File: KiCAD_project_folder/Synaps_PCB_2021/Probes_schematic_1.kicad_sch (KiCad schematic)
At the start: 28 parts, among them U3 LTC2452ITS8-TRMPBF, U4 LTC2452ITS8-TRMPBF, U5 LTC2452ITS8-TRMPBF, U6 LTC2452ITS8-TRMPBF

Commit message: Added library for one piece
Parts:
- renumbered C35 to C12, C36 to C13, C37 to C14, C38 to C15, C39 to C16, C40 to C17, C41 to C18, C42 to C19, C43 to C20, C44 to C21, C45 to C22, C46 to C23, C47 to C24, C48 to C25, C49 to C26, C50 to C27, C51 to C28, C52 to C29, C53 to C30, C54 to C31, C55 to C32, C56 to C33, C57 to C34, C58 to C35, U4 to U?, U5 to U?, U6 to U?, U3 to U?

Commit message: Added LTC2452 librairy
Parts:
- removed U? (x4): LTC2452ITS8-TRMPBF, TSOT-23_TS8_LIT, symbol 2021-11-05_00-54-21:LTC2452ITS8-TRMPBF
- added U3, U4, U5, U6: LTC2452ITS8-TRMPBF, TSOT-23_TS8_LIT, symbol LTC2452:LTC2452ITS8-TRMPBF
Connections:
- net +3V3: now also U3.3 (REF), U3.4 (VCC), U4.3 (REF), U4.4 (VCC), U5.3 (REF), U5.4 (VCC), U6.3 (REF), U6.4 (VCC)
- net GNDREF: now also U3.2 (GND), U3.8 (SDO), U4.2 (GND), U4.8 (SDO), U5.2 (GND), U5.8 (SDO), U6.2 (GND), U6.8 (SDO)
- net Probe1_SDO: now also U3.7 (*CS), U4.7 (*CS), U5.7 (*CS), U6.7 (*CS)
- net Probe1_~{CS}: now also U3.6 (IN+), U4.6 (IN+), U5.6 (IN+), U6.6 (IN+)
- net Probe_SCK: now also U3.1 (SCK), U4.1 (SCK), U5.1 (SCK), U6.1 (SCK)
- net sense_+: now also U3.5 (IN-), U4.5 (IN-), U5.5 (IN-), U6.5 (IN-)
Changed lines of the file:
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@@
     (pin "1")
   )
-  (symbol (lib_id "2021-11-05_00-54-21:LTC2452ITS8-TRMPBF") (at 182.88 39.37 0) (unit 1)
-    (in_bom yes) (on_board yes)
-    (property "Reference" "U?" (id 0) (at 210.82 29.5402 0)
+  (symbol (lib_id "LTC2452:LTC2452ITS8-TRMPBF") (at 53.34 162.56 0) (unit 1)
+    (in_bom yes) (on_board yes) (fields_autoplaced)
+    (property "Reference" "U3" (id 0) (at 81.28 153.3324 0)
       (effects (font (size 1.524 1.524)))
     )
-    (property "Value" "LTC2452ITS8-TRMPBF" (id 1) (at 210.82 32.2326 0)
+    (property "Value" "LTC2452ITS8-TRMPBF" (id 1) (at 81.28 156.3258 0)
+      (effects (font (size 1.524 1.524)))
+    )
+    (property "Footprint" "TSOT-23_TS8_LIT" (id 2) (at 81.28 156.464 0)
+      (effects (font (size 1.524 1.524)) hide)
+    )
+    (property "Datasheet" "" (id 3) (at 53.34 162.56 0)
+      (effects (font (size 1.524 1.524)))
+    )
+    (pin "1")
+    (pin "2")
+    (pin "3")
+    (pin "4")
+    (pin "5")
+    (pin "6")
+    (pin "7")
+    (pin "8")
+  )
+  (symbol (lib_id "LTC2452:LTC2452ITS8-TRMPBF") (at 182.88 134.62 0) (unit 1)
+    (in_bom yes) (on_board yes) (fields_autoplaced)
+    (property "Reference" "U6" (id 0) (at 210.82 125.3924 0)
+      (effects (font (size 1.524 1.524)))
+    )
+    (property "Value" "LTC2452ITS8-TRMPBF" (id 1) (at 210.82 128.3858 0)
+      (effects (font (size 1.524 1.524)))
+    )
+    (property "Footprint" "TSOT-23_TS8_LIT" (id 2) (at 210.82 128.524 0)
+      (effects (font (size 1.524 1.524)) hide)
+    )
+    (property "Datasheet" "" (id 3) (at 182.88 134.62 0)
+      (effects (font (size 1.524 1.524)))
+    )
+    (pin "1")
+    (pin "2")
+    (pin "3")
+    (pin "4")
+    (pin "5")
+    (pin "6")
+    (pin "7")
+    (pin "8")
+  )
+  (symbol (lib_id "LTC2452:LTC2452ITS8-TRMPBF") (at 182.88 88.9 0) (unit 1)
+    (in_bom yes) (on_board yes) (fields_autoplaced)
+    (property "Reference" "U5" (id 0) (at 210.82 79.6724 0)
+      (effects (font (size 1.524 1.524)))
+    )
+    (property "Value" "LTC2452ITS8-TRMPBF" (id 1) (at 210.82 82.6658 0)
+      (effects (font (size 1.524 1.524)))
+    )
+    (property "Footprint" "TSOT-23_TS8_LIT" (id 2) (at 210.82 82.804 0)
+      (effects (font (size 1.524 1.524)) hide)
+    )
+    (property "Datasheet" "" (id 3) (at 182.88 88.9 0)
+      (effects (font (size 1.524 1.524)))
+    )
+    (pin "1")
+    (pin "2")
+    (pin "3")
+    (pin "4")
+    (pin "5")
+    (pin "6")
+    (pin "7")
+    (pin "8")
+  )
+  (symbol (lib_id "LTC2452:LTC2452ITS8-TRMPBF") (at 182.88 39.37 0) (unit 1)
+    (in_bom yes) (on_board yes) (fields_autoplaced)
+    (property "Reference" "U4" (id 0) (at 210.82 30.1424 0)
+      (effects (font (size 1.524 1.524)))
+    )
+    (property "Value" "LTC2452ITS8-TRMPBF" (id 1) (at 210.82 33.1358 0)
       (effects (font (size 1.524 1.524)))
     )
@@
       (effects (font (size 1.524 1.524)))
     )
-  )
-  (symbol (lib_id "2021-11-05_00-54-21:LTC2452ITS8-TRMPBF") (at 182.88 88.9 0) (unit 1)
-    (in_bom yes) (on_board yes)
-    (property "Reference" "U?" (id 0) (at 210.82 79.0702 0)
-      (effects (font (size 1.524 1.524)))
-    )
-    (property "Value" "LTC2452ITS8-TRMPBF" (id 1) (at 210.82 81.7626 0)
-      (effects (font (size 1.524 1.524)))
-    )
-    (property "Footprint" "TSOT-23_TS8_LIT" (id 2) (at 210.82 82.804 0)
-      (effects (font (size 1.524 1.524)) hide)
-    )
-    (property "Datasheet" "" (id 3) (at 182.88 88.9 0)
-      (effects (font (size 1.524 1.524)))
-    )
-  )
-  (symbol (lib_id "2021-11-05_00-54-21:LTC2452ITS8-TRMPBF") (at 182.88 134.62 0) (unit 1)
-    (in_bom yes) (on_board yes)
-    (property "Reference" "U?" (id 0) (at 210.82 124.7902 0)
-      (effects (font (size 1.524 1.524)))
-    )
-    (property "Value" "LTC2452ITS8-TRMPBF" (id 1) (at 210.82 127.4826 0)
-      (effects (font (size 1.524 1.524)))
-    )
-    (property "Footprint" "TSOT-23_TS8_LIT" (id 2) (at 210.82 128.524 0)
-      (effects (font (size 1.524 1.524)) hide)
-    )
-    (property "Datasheet" "" (id 3) (at 182.88 134.62 0)
-      (effects (font (size 1.524 1.524)))
-    )
-  )
-  (symbol (lib_id "2021-11-05_00-54-21:LTC2452ITS8-TRMPBF") (at 53.34 162.56 0) (unit 1)
-    (in_bom yes) (on_board yes)
-    (property "Reference" "U?" (id 0) (at 81.28 152.7302 0)
-      (effects (font (size 1.524 1.524)))
-    )
-    (property "Value" "LTC2452ITS8-TRMPBF" (id 1) (at 81.28 155.4226 0)
-      (effects (font (size 1.524 1.524)))
-    )
-    (property "Footprint" "TSOT-23_TS8_LIT" (id 2) (at 81.28 156.464 0)
-      (effects (font (size 1.524 1.524)) hide)
-    )
-    (property "Datasheet" "" (id 3) (at 53.34 162.56 0)
-      (effects (font (size 1.524 1.524)))
-    )
+    (pin "1")
+    (pin "2")
+    (pin "3")
+    (pin "4")
+    (pin "5")
+    (pin "6")
+    (pin "7")
+    (pin "8")
   )
 )

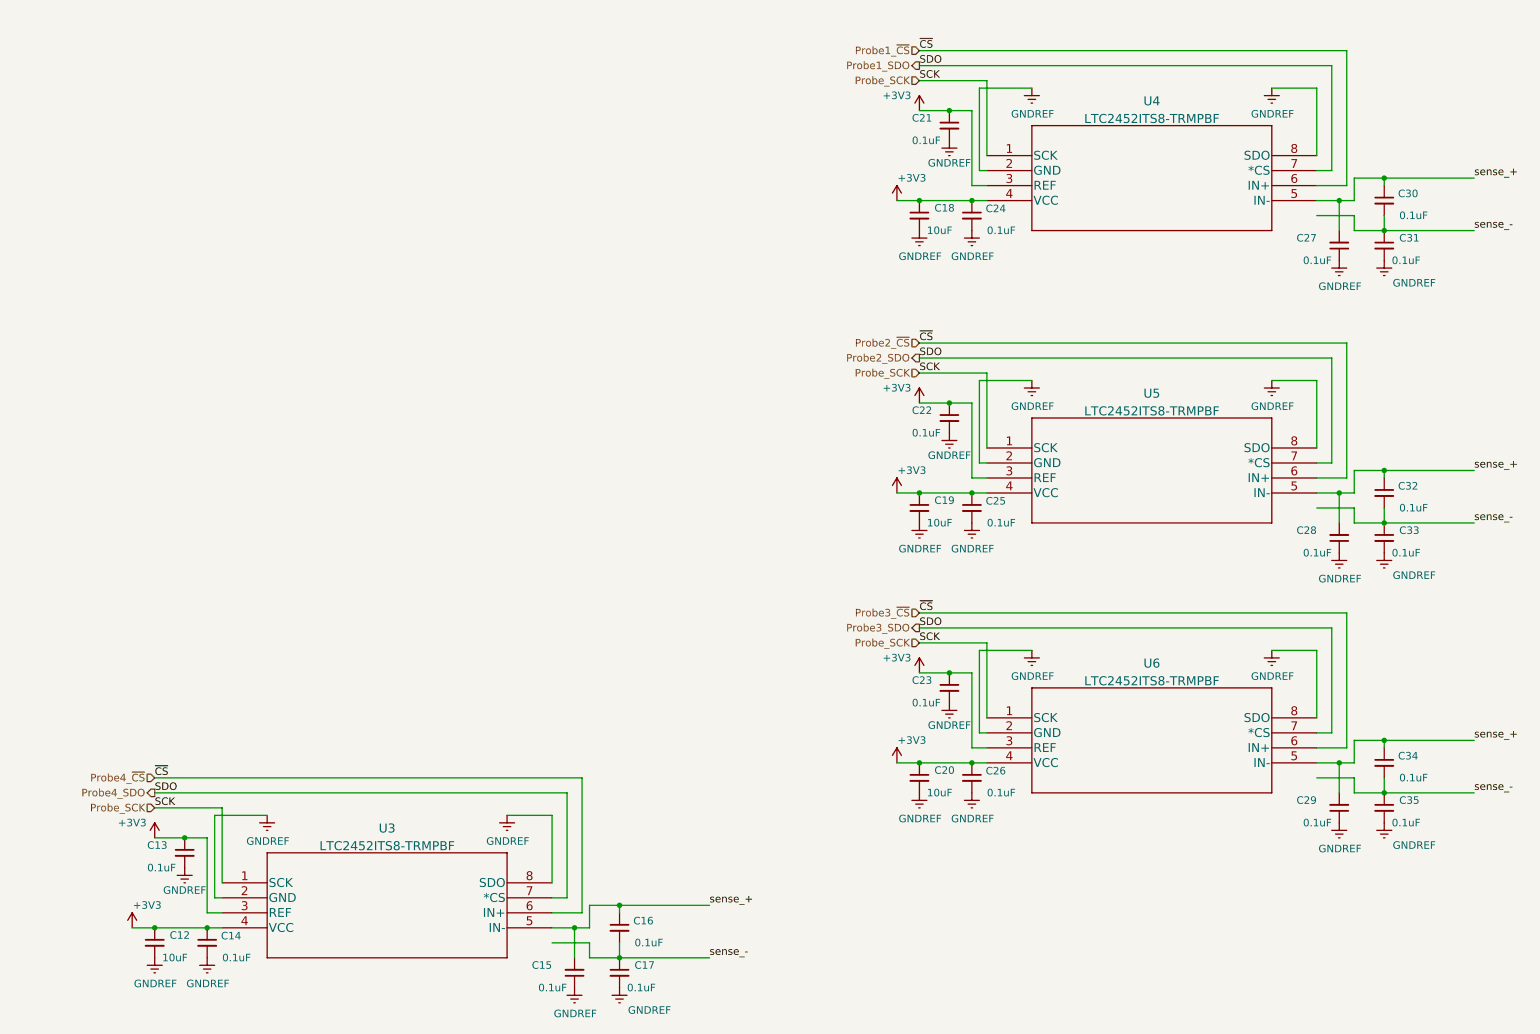
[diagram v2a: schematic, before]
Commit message: Inertia measurement unit schematic
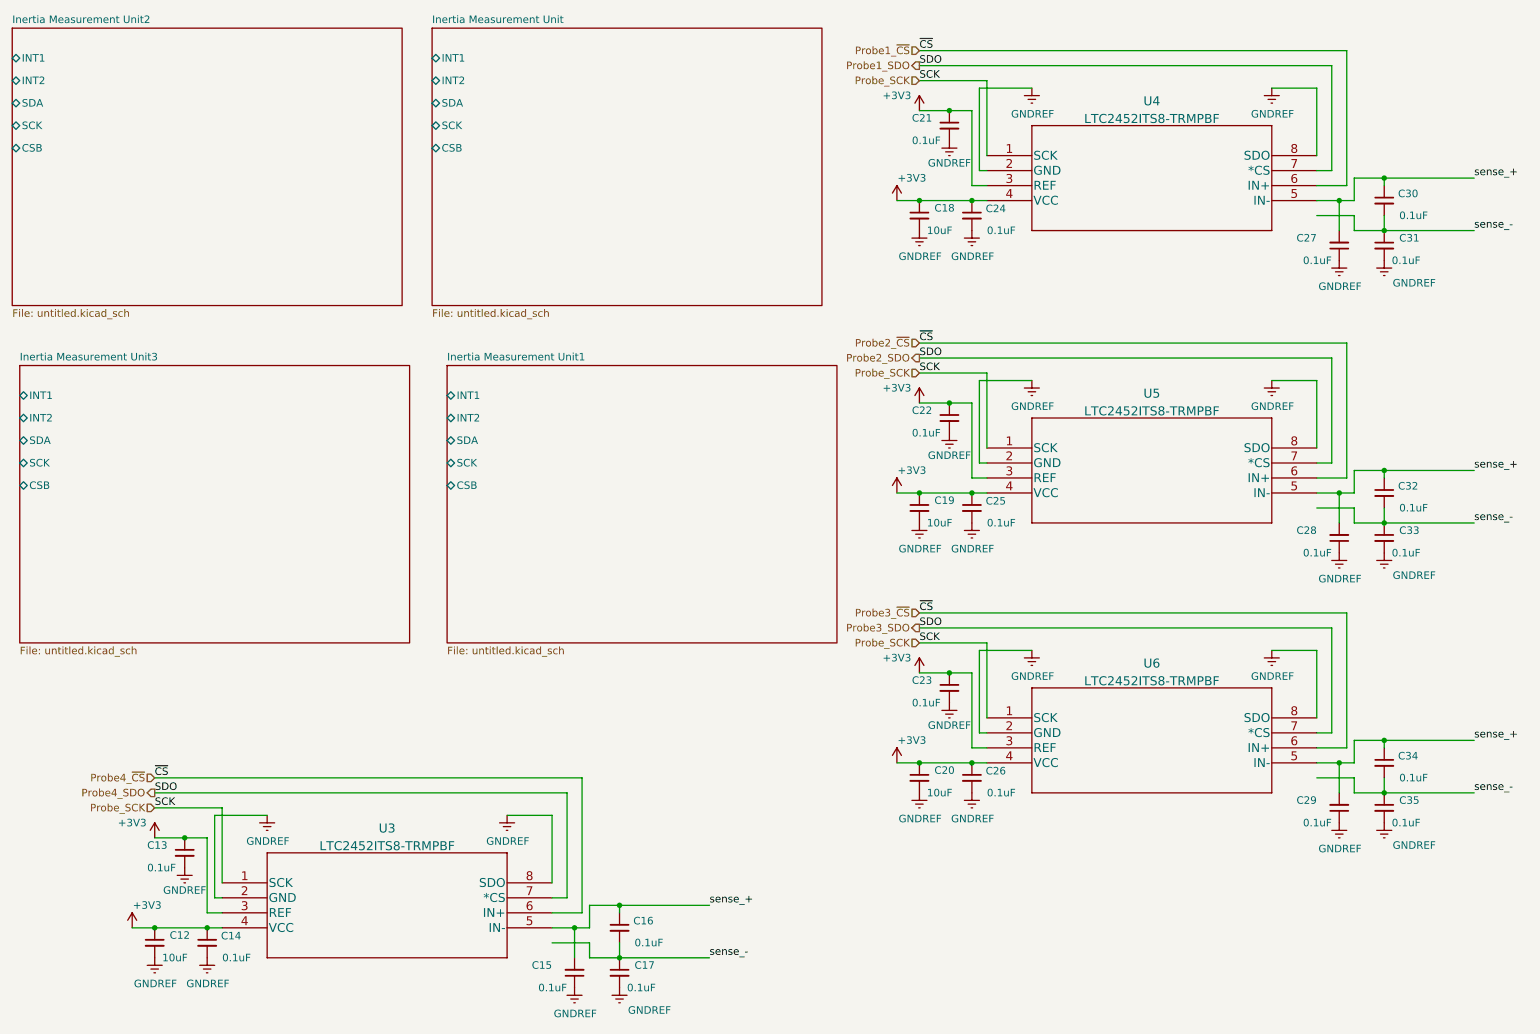
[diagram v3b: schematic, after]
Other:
- added sheet Inertia Measurement Unit (untitled.kicad_sch)
- added sheet Inertia Measurement Unit1 (untitled.kicad_sch)
- added sheet Inertia Measurement Unit2 (untitled.kicad_sch)
- added sheet Inertia Measurement Unit3 (untitled.kicad_sch)
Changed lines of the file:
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@@
     (pin "8")
   )
+  (sheet (at 88.9 17.78) (size 66.04 46.99) (fields_autoplaced)
+    (stroke (width 0.1524) (type solid) (color 0 0 0 0))
+    (fill (color 0 0 0 0.0000))
+    (property "Sheet name" "Inertia Measurement Unit" (id 0) (at 88.9 17.0684 0)
+      (effects (font (size 1.27 1.27)) (justify left bottom))
+    )
+    (property "Sheet file" "untitled.kicad_sch" (id 1) (at 88.9 65.3546 0)
+      (effects (font (size 1.27 1.27)) (justify left top))
+    )
+    (pin "INT1" bidirectional (at 88.9 22.86 180)
+      (effects (font (size 1.27 1.27)) (justify left))
+    )
+    (pin "INT2" bidirectional (at 88.9 26.67 180)
+      (effects (font (size 1.27 1.27)) (justify left))
+    )
+    (pin "SDA" bidirectional (at 88.9 30.48 180)
+      (effects (font (size 1.27 1.27)) (justify left))
+    )
+    (pin "SCK" bidirectional (at 88.9 34.29 180)
+      (effects (font (size 1.27 1.27)) (justify left))
+    )
+    (pin "CSB" bidirectional (at 88.9 38.1 180)
+      (effects (font (size 1.27 1.27)) (justify left))
+    )
+  )
+  (sheet (at 17.78 17.78) (size 66.04 46.99) (fields_autoplaced)
+    (stroke (width 0.1524) (type solid) (color 0 0 0 0))
+    (fill (color 0 0 0 0.0000))
+    (property "Sheet name" "Inertia Measurement Unit2" (id 0) (at 17.78 17.0684 0)
+      (effects (font (size 1.27 1.27)) (justify left bottom))
+    )
+    (property "Sheet file" "untitled.kicad_sch" (id 1) (at 17.78 65.3546 0)
+      (effects (font (size 1.27 1.27)) (justify left top))
+    )
+    (pin "INT1" bidirectional (at 17.78 22.86 180)
+      (effects (font (size 1.27 1.27)) (justify left))
+    )
+    (pin "INT2" bidirectional (at 17.78 26.67 180)
+      (effects (font (size 1.27 1.27)) (justify left))
+    )
+    (pin "SDA" bidirectional (at 17.78 30.48 180)
+      (effects (font (size 1.27 1.27)) (justify left))
+    )
+    (pin "SCK" bidirectional (at 17.78 34.29 180)
+      (effects (font (size 1.27 1.27)) (justify left))
+    )
+    (pin "CSB" bidirectional (at 17.78 38.1 180)
+      (effects (font (size 1.27 1.27)) (justify left))
+    )
+  )
+  (sheet (at 91.44 74.93) (size 66.04 46.99) (fields_autoplaced)
+    (stroke (width 0.1524) (type solid) (color 0 0 0 0))
+    (fill (color 0 0 0 0.0000))
+    (property "Sheet name" "Inertia Measurement Unit1" (id 0) (at 91.44 74.2184 0)
+      (effects (font (size 1.27 1.27)) (justify left bottom))
+    )
+    (property "Sheet file" "untitled.kicad_sch" (id 1) (at 91.44 122.5046 0)
+      (effects (font (size 1.27 1.27)) (justify left top))
+    )
+    (pin "INT1" bidirectional (at 91.44 80.01 180)
+      (effects (font (size 1.27 1.27)) (justify left))
+    )
+    (pin "INT2" bidirectional (at 91.44 83.82 180)
+      (effects (font (size 1.27 1.27)) (justify left))
+    )
+    (pin "SDA" bidirectional (at 91.44 87.63 180)
+      (effects (font (size 1.27 1.27)) (justify left))
+    )
+    (pin "SCK" bidirectional (at 91.44 91.44 180)
+      (effects (font (size 1.27 1.27)) (justify left))
+    )
+    (pin "CSB" bidirectional (at 91.44 95.25 180)
+      (effects (font (size 1.27 1.27)) (justify left))
+    )
+  )
+  (sheet (at 19.05 74.93) (size 66.04 46.99) (fields_autoplaced)
+    (stroke (width 0.1524) (type solid) (color 0 0 0 0))
+    (fill (color 0 0 0 0.0000))
+    (property "Sheet name" "Inertia Measurement Unit3" (id 0) (at 19.05 74.2184 0)
+      (effects (font (size 1.27 1.27)) (justify left bottom))
+    )
+    (property "Sheet file" "untitled.kicad_sch" (id 1) (at 19.05 122.5046 0)
+      (effects (font (size 1.27 1.27)) (justify left top))
+    )
+    (pin "INT1" bidirectional (at 19.05 80.01 180)
+      (effects (font (size 1.27 1.27)) (justify left))
+    )
+    (pin "INT2" bidirectional (at 19.05 83.82 180)
+      (effects (font (size 1.27 1.27)) (justify left))
+    )
+    (pin "SDA" bidirectional (at 19.05 87.63 180)
+      (effects (font (size 1.27 1.27)) (justify left))
+    )
+    (pin "SCK" bidirectional (at 19.05 91.44 180)
+      (effects (font (size 1.27 1.27)) (justify left))
+    )
+    (pin "CSB" bidirectional (at 19.05 95.25 180)
+      (effects (font (size 1.27 1.27)) (justify left))
+    )
+  )
 )

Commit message: Added basic PCB guidelines
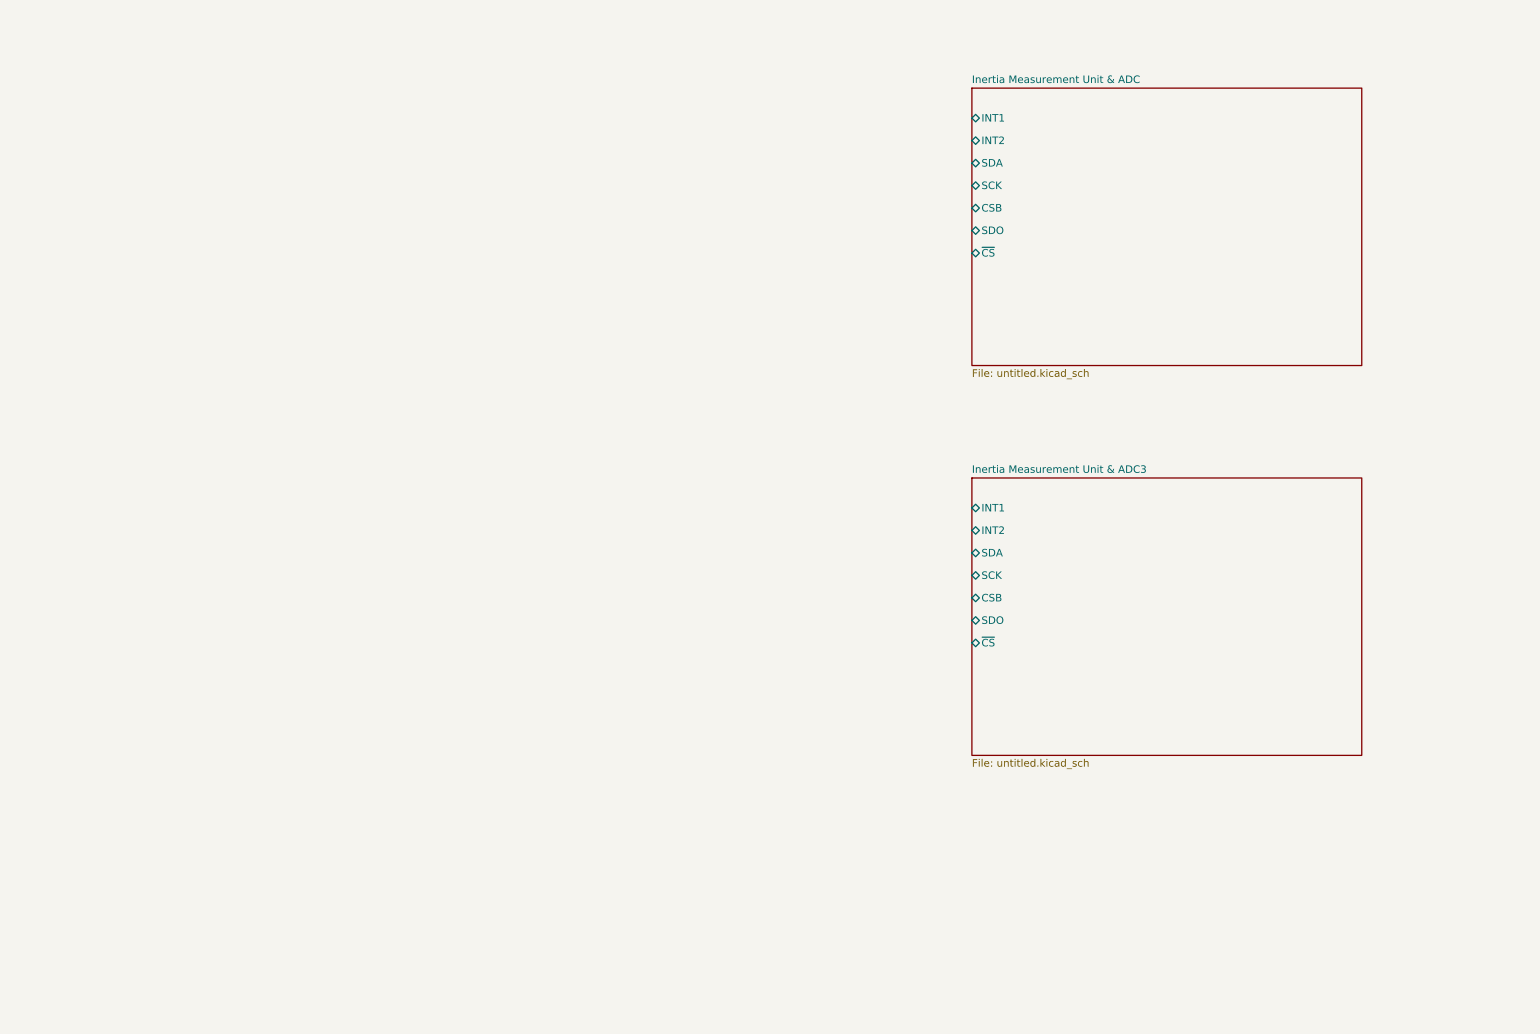
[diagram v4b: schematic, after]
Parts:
- removed C12, C18, C19, C20: 10uF, symbol Device:C_Small
- removed C13, C14, C15, C16, C17, C21, C22, C23, C24, C25, C26, C27, C28, C29, C30, C31, C32, C33, C34, C35: 0.1uF, symbol Device:C_Small
- removed U3, U4, U5, U6: LTC2452ITS8-TRMPBF, TSOT-23_TS8_LIT, symbol LTC2452:LTC2452ITS8-TRMPBF
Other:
- sheet Inertia Measurement Unit2 renamed Inertia Measurement Unit & ADC
- removed sheet Inertia Measurement Unit
- removed sheet Inertia Measurement Unit1
- removed sheet Inertia Measurement Unit3
- added sheet Inertia Measurement Unit & ADC3 (untitled.kicad_sch)
- sheet Inertia Measurement Unit & ADC ports: added SDO, ~{CS}; removed none
